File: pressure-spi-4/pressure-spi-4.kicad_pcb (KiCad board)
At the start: 2 copper layers, 45.7 x 17.8 mm, 14 parts, among them J1 Conn_01x08_Male, U1 TruStability_SPI_RR, U2 TruStability_SPI_RR, U3 TruStability_SPI_RR, U4 TruStability_SPI_RN

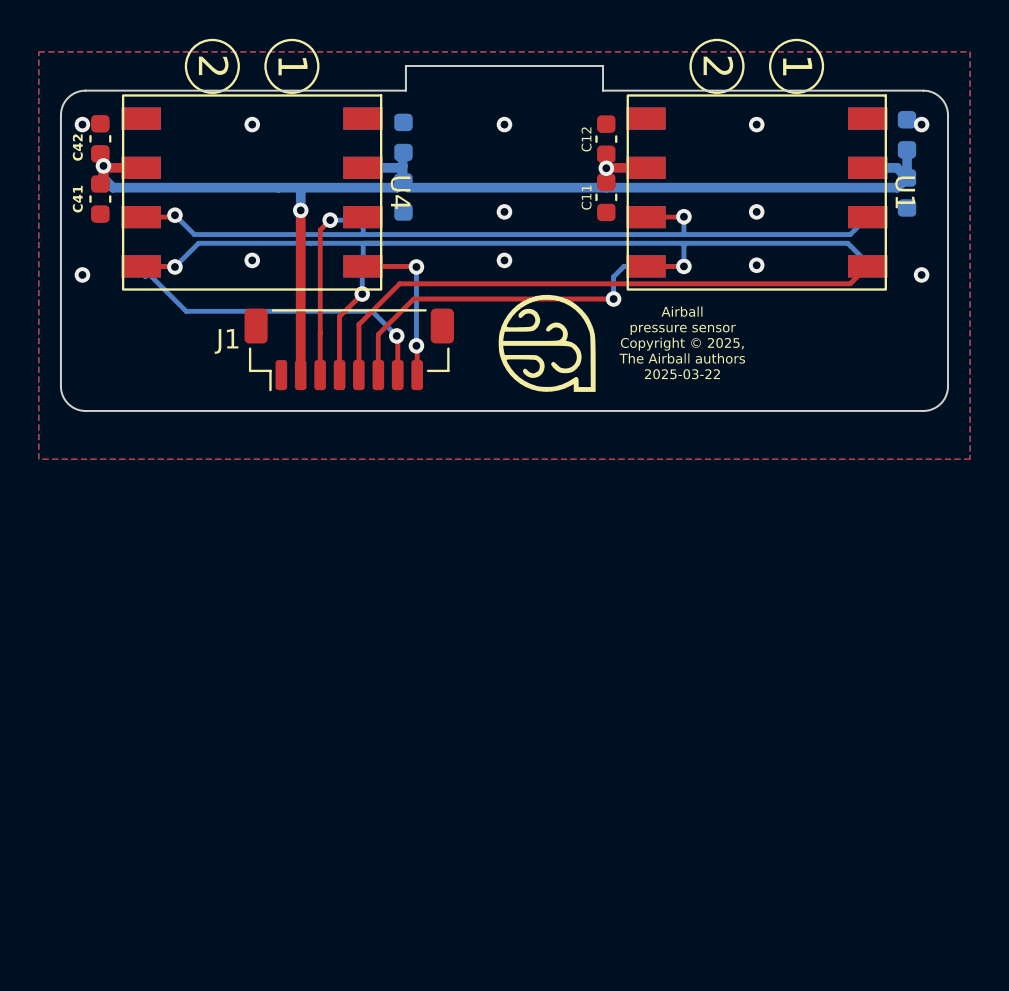
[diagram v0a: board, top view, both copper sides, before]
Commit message: Designed and routed board.
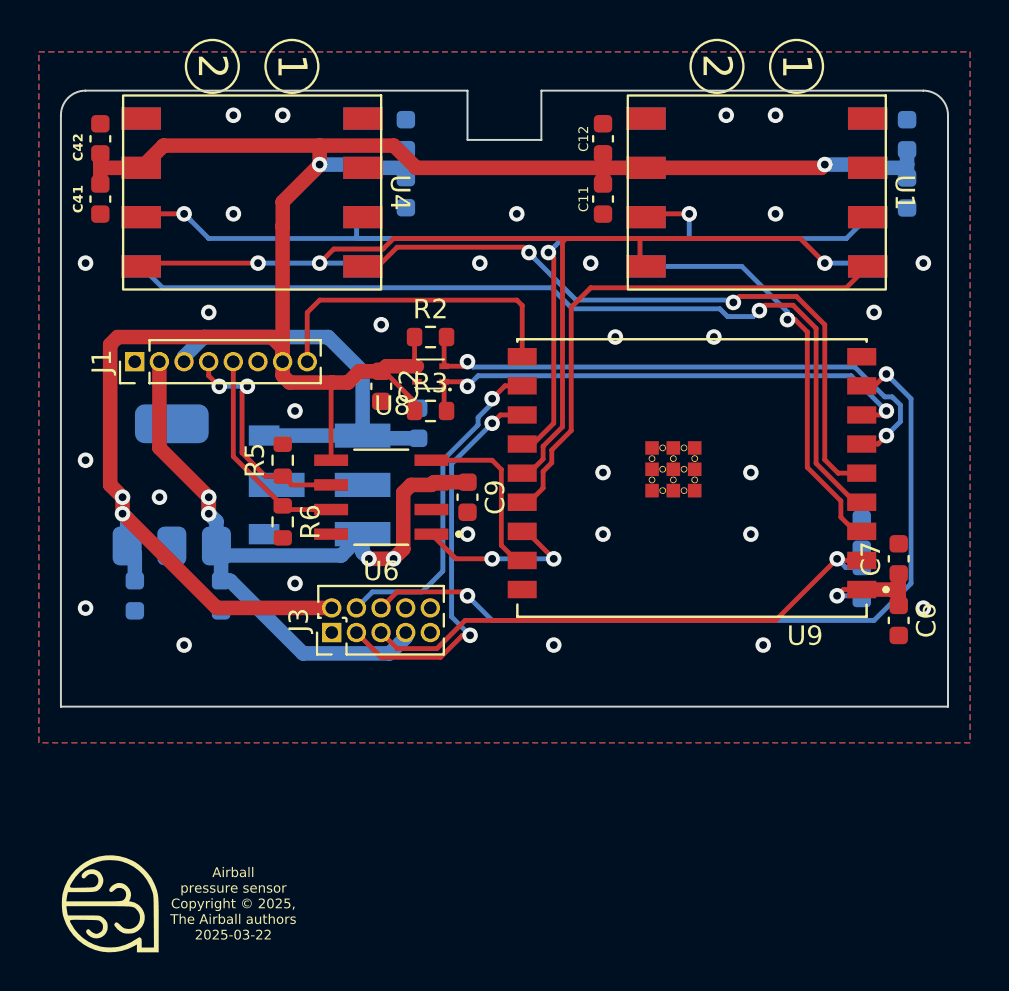
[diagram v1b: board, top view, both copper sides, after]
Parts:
- added C1: 10uF, Capacitor_SMD:C_0603_1608Metric, B.Cu at (-4.45, 17.1)
- added C2: 10 uF, Capacitor_SMD:C_0603_1608Metric, F.Cu at (-6.35, 15.2)
- added C3: 10uF, Capacitor_SMD:C_0603_1608Metric, B.Cu at (-14.6, 26.0)
- added C4: 1uF, Capacitor_SMD:C_0603_1608Metric, B.Cu at (18.4, 22.9)
- added C5: 10uF, Capacitor_SMD:C_0603_1608Metric, B.Cu at (-19.1, 26.0)
- added C6: 10uF, Capacitor_SMD:C_0603_1608Metric, F.Cu at (20.3, 27.3)
- added C7: 0.1uF, Capacitor_SMD:C_0603_1608Metric, F.Cu at (20.3, 24.1)
- added C9: 10uF, Capacitor_SMD:C_0603_1608Metric, F.Cu at (-1.91, 21.0)
- added J3: Conn_02x05_Odd_Even, Connector_PinHeader_1.27mm:PinHeader_2x05_P1.27mm_Vertical, F.Cu at (-8.90, 27.9)
- added PS1: K7805MT-500R4, airball-hardware:CONV_K7805MT-500R4, B.Cu at (-9.53, 20.3)
- added R1: 10k, Resistor_SMD:R_0603_1608Metric, B.Cu at (18.4, 25.4)
- added R2: 4.7k, Resistor_SMD:R_0603_1608Metric, F.Cu at (-3.81, 12.7)
- added R3: 4.7k, Resistor_SMD:R_0603_1608Metric, F.Cu at (-3.81, 16.5)
- added R5: 60Ω, Resistor_SMD:R_0603_1608Metric, F.Cu at (-11.4, 19.1)
- added R6: 60Ω, Resistor_SMD:R_0603_1608Metric, F.Cu at (-11.4, 22.2)
- added U6: TJA1051T_3_118, airball-hardware:TJA1051T_3_118, F.Cu at (-6.35, 21.0)
- added U7: LT1963AxST-3.3, Package_TO_SOT_SMD:SOT-223-3_TabPin2, B.Cu at (-17.1, 20.3)
- added U8: SHT40-BD1B-R3, airball-hardware:SHT4X humidity sensor, F.Cu at (-3.81, 14.6)
- added U9: ESP32-C3-WROOM-02U-N4, airball-hardware:XCVR_ESP32-C3-WROOM-02U-N4, F.Cu at (9.66, 20.0)
- J1: value Conn_01x08_Male -> Conn_01x08_Socket; footprint airball-hardware:JST_SH_BM08B-SRSS-TB_1x08-1MP_P1.00mm_Vertical -> Connector_PinHeader_1.27mm:PinHeader_1x08_P1.27mm_Vertical
- moved G*** 36.6 mm to (-20.3, 41.9)
- moved J1 11.1 mm to (-19.1, 14.0), turned to 90 degrees
- moved C31 0.26 mm to (-5.08, 5.26)
- moved C11 0.19 mm to (5.08, 5.59)
- moved C32 0.19 mm to (-5.08, 2.27)
- moved C12 0.17 mm to (5.08, 2.48)
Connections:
- J1 pad 2: +3V3 -> VBAT_5V
- J1 pad 3: /MISO -> 12V28
- J1 pad 4: /SCLK -> CANL
- J1 pad 5: /!CS1 -> CANH
- J1 pad 6: /!CS2 -> GND
- J1 pad 7: /!CS3 -> +3V3
- J1 pad 8: /!CS4 -> 1WIRE_DQ
- U1 pad 3: /MISO -> MISO
- U1 pad 4: /SCLK -> SCLK
- U1 pad 5: /!CS1 -> !CS1
- U2 pad 3: /MISO -> MISO
- U2 pad 4: /SCLK -> SCLK
- U2 pad 5: /!CS2 -> !CS2
- U3 pad 3: /MISO -> MISO
- U3 pad 4: /SCLK -> SCLK
- U3 pad 5: /!CS3 -> !CS3
- U4 pad 3: /MISO -> MISO
- U4 pad 4: /SCLK -> SCLK
- U4 pad 5: /!CS4 -> !CS4
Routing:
- net MISO: track 0.00 -> 58.3 mm, vias 0 -> 3
- net +3V3: track 66.7 -> 123.8 mm, vias 3 -> 5
- net SCLK: track 0.00 -> 57.0 mm, vias 0 -> 3
- net /MISO: track 52.3 -> 0.00 mm, vias 3 -> 0
- net /SCLK: track 50.0 -> 0.00 mm, vias 3 -> 0
- net !CS3: track 0.00 -> 46.7 mm, vias 0 -> 1
- net VBAT_5V: track 0.00 -> 43.1 mm, vias 0 -> 4
- net MCU_IO9: track 0.00 -> 41.9 mm, vias 0 -> 2
- net !CS4: track 0.00 -> 35.3 mm, vias 0 -> 2
- net /!CS1: track 30.1 -> 0.00 mm
- net MCU_EN: track 0.00 -> 29.5 mm, vias 0 -> 1
- net SDA: track 0.00 -> 29.4 mm, vias 0 -> 2
- net !CS1: track 0.00 -> 27.5 mm
- net SCL: track 0.00 -> 26.8 mm, vias 0 -> 2
- net 12V28: track 0.00 -> 21.9 mm
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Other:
- board size 45.7 x 17.8 mm -> 45.7 x 31.8 mm

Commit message: Ongoing changes.
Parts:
- moved G*** 13.5 mm to (-19.1, 28.4)
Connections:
- U9 pad 20_1: (no net) -> GND
- U9 pad 20_10: (no net) -> GND
- U9 pad 20_11: (no net) -> GND
- U9 pad 20_12: (no net) -> GND
- U9 pad 20_2: (no net) -> GND
- U9 pad 20_3: (no net) -> GND
- U9 pad 20_4: (no net) -> GND
- U9 pad 20_5: (no net) -> GND
- U9 pad 20_6: (no net) -> GND
- U9 pad 20_7: (no net) -> GND
- U9 pad 20_8: (no net) -> GND
- U9 pad 20_9: (no net) -> GND
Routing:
- net +3V3: track 123.8 -> 162.6 mm
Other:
- outline, holes or cut-outs redrawn
